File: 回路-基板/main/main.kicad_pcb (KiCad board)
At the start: 2 copper layers, 60 x 60 mm, 47 parts, among them J1 Conn_01x07_Pin, J2 Conn_01x08_Pin, J3 Conn_01x08_Pin, J4 Conn_01x08_Pin, J5 Conn_01x08_Pin, M1 Jumper_2_Small_Open, M2 Jumper_2_Small_Open, M3 Jumper_2_Small_Open, SW1 SW_Push, SW2 SW_Push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

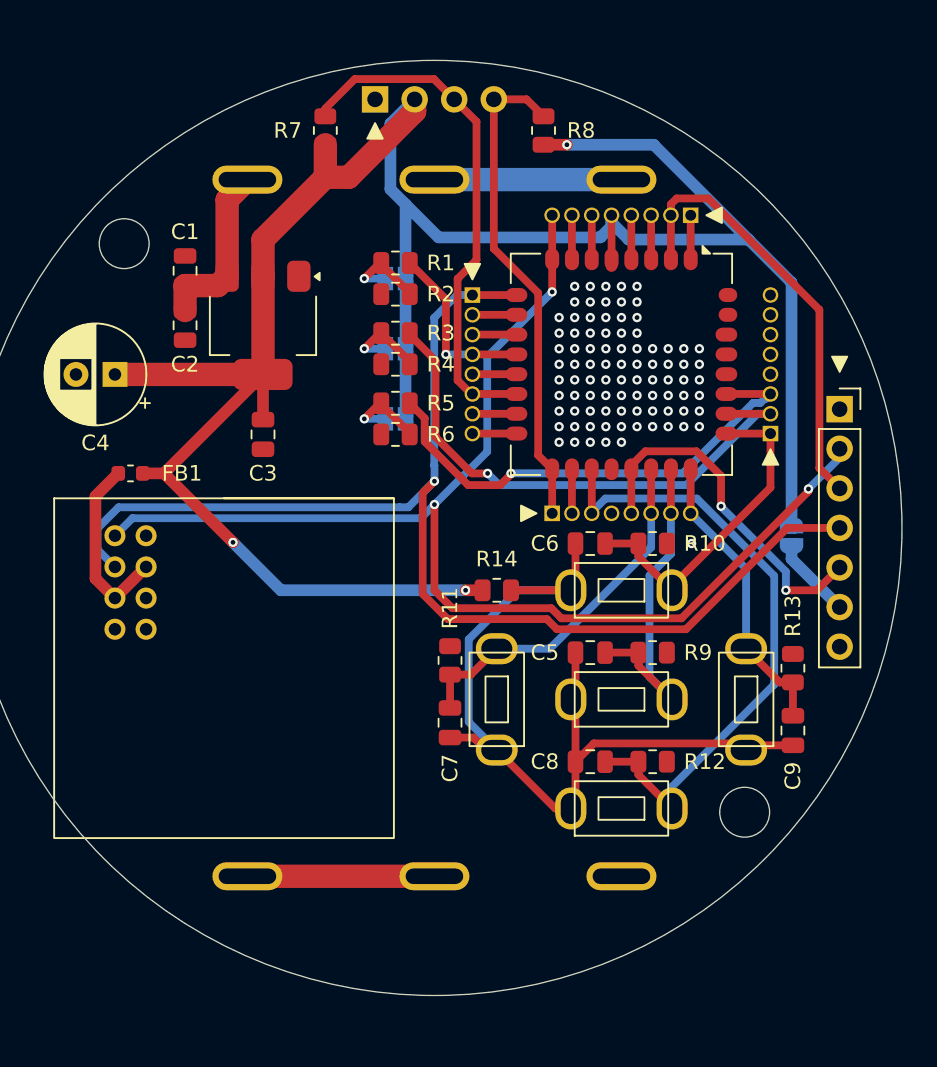
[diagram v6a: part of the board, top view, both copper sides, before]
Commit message: メインのPCBを更新した
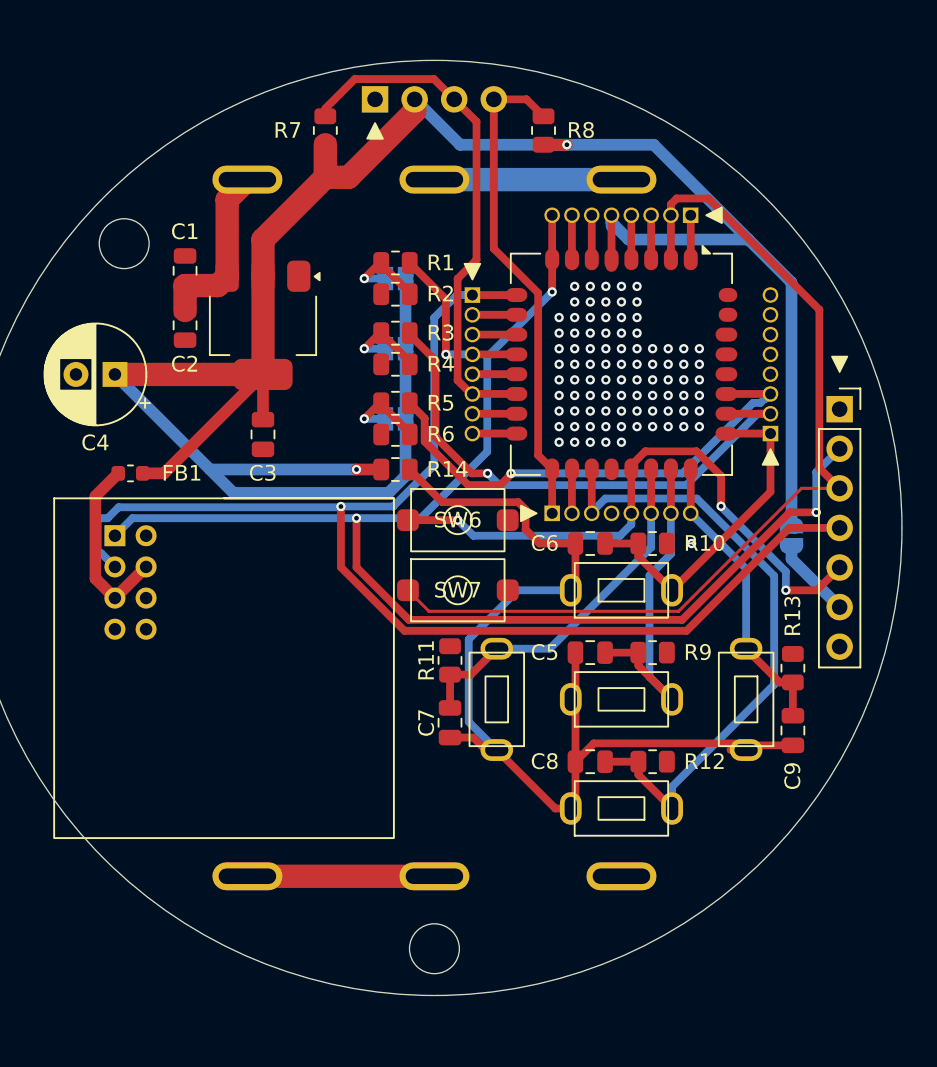
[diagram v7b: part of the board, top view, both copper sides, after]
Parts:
- added SW6: SW_Push, @2024-cansat:Tactile1, F.Cu at (1.50, -0.50)
- added SW7: SW_Push, @2024-cansat:Tactile1, F.Cu at (1.50, 4.00)
- moved REF** 21.7 mm to (0.00, 27.0), turned to -45 degrees
- moved R14 10.1 mm to (-2.50, -3.75)
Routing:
- net 2: track 28.2 -> 59.7 mm
- net 21: track 23.0 -> 38.7 mm, vias 2 -> 3
- net Net-(C5-Pad1): track 58.4 -> 67.9 mm
- net 8: track 80.2 -> 84.6 mm
- net +3.3V: track 155.7 -> 153.1 mm, vias 3 -> 2
- net 9: track 80.1 -> 82.4 mm

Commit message: JLCPCB用の出力ファイルなどを追加
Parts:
- R10, R11, R12, R13, R9: value 100k -> 10K
- R14: value 10k -> 1K
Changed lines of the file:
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@@
 		(sheetname "ルート")
 		(sheetfile "main.kicad_sch")
-		(attr smd)
+		(attr smd exclude_from_pos_files exclude_from_bom)
 		(fp_line
 			(start -1.85 3.41)
@@
 		(sheetname "ルート")
 		(sheetfile "main.kicad_sch")
-		(attr through_hole)
+		(attr through_hole exclude_from_pos_files exclude_from_bom)
 		(fp_poly
 			(pts
@@
 			)
 		)
-		(property "Value" "100k"
+		(property "Value" "10K"
 			(at 0 1.65 90)
 			(layer "F.Fab")
@@
 			)
 		)
-		(property "Value" "100k"
+		(property "Value" "10K"
 			(at 0 1.65 180)
 			(layer "F.Fab")
@@
 		(sheetname "ルート")
 		(sheetfile "main.kicad_sch")
-		(attr through_hole)
+		(attr through_hole exclude_from_pos_files exclude_from_bom)
 		(fp_rect
 			(start 3 -1.75)
@@
 		(sheetname "ルート")
 		(sheetfile "main.kicad_sch")
-		(attr through_hole)
+		(attr through_hole exclude_from_pos_files exclude_from_bom)
 		(fp_poly
 			(pts
@@
 		(tags "resistor")
 		(property "Reference" "R14"
-			(at 2 0 360)
+			(at 2 0 0)
 			(layer "F.SilkS")
 			(effects
@@
 			)
 		)
-		(property "Value" "10k"
-			(at 0 1.65 360)
+		(property "Value" "1K"
+			(at 0 1.65 0)
 			(layer "F.Fab")
 			(effects
@@
 		)
 		(fp_text user "${REFERENCE}"
-			(at 0 0 360)
+			(at 0 0 0)
 			(layer "F.Fab")
 			(effects
@@
 		(sheetname "ルート")
 		(sheetfile "main.kicad_sch")
-		(attr through_hole)
+		(attr through_hole exclude_from_pos_files exclude_from_bom)
 		(fp_poly
 			(pts
@@
 		(sheetname "ルート")
 		(sheetfile "main.kicad_sch")
-		(attr through_hole)
+		(attr through_hole exclude_from_pos_files exclude_from_bom)
 		(fp_rect
 			(start -1.475 -0.725)
@@
 		(sheetname "ルート")
 		(sheetfile "main.kicad_sch")
-		(attr through_hole)
+		(attr through_hole exclude_from_pos_files exclude_from_bom)
 		(fp_poly
 			(pts
@@
 		(sheetname "ルート")
 		(sheetfile "main.kicad_sch")
-		(attr through_hole)
+		(attr through_hole exclude_from_pos_files exclude_from_bom)
 		(fp_rect
 			(start 3 -1.75)
@@
 			)
 		)
-		(property "Value" "100k"
+		(property "Value" "10K"
 			(at 0 1.65 90)
 			(layer "F.Fab")
@@
 		(sheetname "ルート")
 		(sheetfile "main.kicad_sch")
-		(attr through_hole)
+		(attr through_hole exclude_from_pos_files exclude_from_bom)
 		(fp_poly
 			(pts
@@
 			)
 		)
-		(property "Value" "100k"
+		(property "Value" "10K"
 			(at 0 1.65 180)
 			(layer "F.Fab")
@@
 		(sheetname "ルート")
 		(sheetfile "main.kicad_sch")
-		(attr through_hole)
+		(attr through_hole exclude_from_pos_files exclude_from_bom)
 		(fp_rect
 			(start 3 -1.75)
@@
 		(sheetname "ルート")
 		(sheetfile "main.kicad_sch")
-		(attr through_hole)
+		(attr through_hole exclude_from_pos_files exclude_from_bom)
 		(fp_poly
 			(pts
@@
 		(sheetname "ルート")
 		(sheetfile "main.kicad_sch")
-		(attr through_hole)
+		(attr through_hole exclude_from_pos_files exclude_from_bom)
 		(fp_rect
 			(start -1.475 -0.725)
@@
 		(sheetname "ルート")
 		(sheetfile "main.kicad_sch")
-		(attr smd)
+		(attr smd exclude_from_pos_files exclude_from_bom)
 		(fp_line
 			(start -7.1 7.1)
@@
 		(sheetname "ルート")
 		(sheetfile "main.kicad_sch")
-		(attr through_hole)
+		(attr through_hole exclude_from_pos_files exclude_from_bom)
 		(fp_line
 			(start -1.33 1.27)
@@
 			)
 		)
-		(property "Value" "100k"
+		(property "Value" "10K"
 			(at 0 1.65 180)
 			(layer "F.Fab")
@@
 		(sheetname "ルート")
 		(sheetfile "main.kicad_sch")
-		(attr smd)
+		(attr smd exclude_from_pos_files exclude_from_bom)
 		(fp_line
 			(start -0.162779 0.51)
@@
 		(sheetname "ルート")
 		(sheetfile "main.kicad_sch")
-		(attr through_hole)
+		(attr through_hole exclude_from_pos_files exclude_from_bom)
 		(fp_line
 			(start 4.491 -0.402)
@@
 		(sheetname "ルート")
 		(sheetfile "main.kicad_sch")
-		(attr through_hole)
+		(attr through_hole exclude_from_pos_files exclude_from_bom)
 		(fp_rect
 			(start 44.6 -5.25)
@@
 		)
 		(zone_connect 1)
-		(attr exclude_from_pos_files)
+		(attr exclude_from_pos_files exclude_from_bom)
 		(fp_line
 			(start -1.4 0.3)
@@
 		)
 		(zone_connect 1)
-		(attr exclude_from_pos_files)
+		(attr exclude_from_pos_files exclude_from_bom)
 		(fp_line
 			(start -1.4 0.3)
@@
 		(sheetname "ルート")
 		(sheetfile "main.kicad_sch")
-		(attr through_hole)
+		(attr through_hole exclude_from_pos_files exclude_from_bom)
 		(fp_rect
 			(start -1.75 -0.25)
@@
 		(sheetname "ルート")
 		(sheetfile "main.kicad_sch")
-		(attr through_hole)
+		(attr through_hole exclude_from_pos_files exclude_from_bom)
 		(fp_rect
 			(start -1.75 -0.25)
@@
 		)
 		(zone_connect 1)
-		(attr exclude_from_pos_files)
+		(attr exclude_from_pos_files exclude_from_bom)
 		(fp_line
 			(start -1.4 0.3)
